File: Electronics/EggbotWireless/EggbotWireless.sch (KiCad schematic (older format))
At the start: 47 parts, among them J1 BATT, J2 Conn_01x04_Female, J3 USB_B_Micro, J4 AVR-ISP-6, Q1 FDD8447L, Q2 FDD8447L, U1 TPS62203DBV, U2 ATmega16A-AU, U3 DW01, U4 FS8205A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

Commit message: pcb prototype v0.1 (no steppers yet)
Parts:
- removed Q2: FDD8447L, Package_TO_SOT_SMD:TO-252-2, symbol Device:Q_NMOS_GDS
- added A1, A2: Pololu_Breakout_A4988, Module:Pololu_Breakout-16_15.2x20.3mm, symbol Driver_Motor:Pololu_Breakout_A4988
- added C14, C15: 100nf, Capacitor_SMD:C_0805_2012Metric_Pad1.15x1.40mm_HandSolder, symbol EggbotWireless-rescue:C-Device-Catfi-rescue
- added J5: Conn_01x03_Female, Connector_PinSocket_2.54mm:PinSocket_1x03_P2.54mm_Vertical, symbol Connector:Conn_01x03_Female
- added M1, M2: Stepper_Motor_bipolar, Connector_PinSocket_2.54mm:PinSocket_1x04_P2.54mm_Horizontal, symbol Motor:Stepper_Motor_bipolar
- added R17, R18: 10K, Resistor_SMD:R_0805_2012Metric_Pad1.15x1.40mm_HandSolder, symbol EggbotWireless-rescue:R-Device-Catfi-rescue
- U5: value INTERFACE-CP2102-GMR(QFN28) -> CP2102-GMR
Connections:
- net labels added: SCL, SDA
- wire segments 160 -> 165
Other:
- moved on the sheet: C7, C8, J2, J3, R6, R7, U5, U6

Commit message: change stepper driver to drv8825
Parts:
- removed A1, A2: Pololu_Breakout_A4988, Module:Pololu_Breakout-16_15.2x20.3mm, symbol Driver_Motor:Pololu_Breakout_A4988
- added A1, A2: Pololu_Breakout_DRV8825, Module:Pololu_Breakout-16_15.2x20.3mm, symbol Driver_Motor:Pololu_Breakout_DRV8825
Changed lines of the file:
@@
-	1    0    0    -1
-$EndComp
-$Comp
-L Driver_Motor:Pololu_Breakout_A4988 A1
-U 1 1 5CE85B52
-P 5100 3550
-F 0 "A1" H 5150 4431 50  0000 C CNN
-F 1 "Pololu_Breakout_A4988" H 5150 4340 50  0000 C CNN
-F 2 "Module:Pololu_Breakout-16_15.2x20.3mm" H 5375 2800 50  0001 L CNN
-F 3 "https://www.pololu.com/product/2980/pictures" H 5200 3250 50  0001 C CNN
-	1    5100 3550
 	1    0    0    -1
 $EndComp
@@
 	1    3600 2800
 	-1   0    0    1
-$EndComp
-$Comp
-L Driver_Motor:Pololu_Breakout_A4988 A2
-U 1 1 5CE843A9
-P 5150 5500
-F 0 "A2" H 5200 6381 50  0000 C CNN
-F 1 "Pololu_Breakout_A4988" H 5200 6290 50  0000 C CNN
-F 2 "Module:Pololu_Breakout-16_15.2x20.3mm" H 5425 4750 50  0001 L CNN
-F 3 "https://www.pololu.com/product/2980/pictures" H 5250 5200 50  0001 C CNN
-	1    5150 5500
-	1    0    0    -1
 $EndComp
 $Comp
@@
 Wire Wire Line
 	9100 5150 9100 5250
+$Comp
+L Driver_Motor:Pololu_Breakout_DRV8825 A1
+U 1 1 5CE88FAE
+P 5050 4150
+F 0 "A1" H 5050 4931 50  0000 C CNN
+F 1 "Pololu_Breakout_DRV8825" H 5050 4840 50  0000 C CNN
+F 2 "Module:Pololu_Breakout-16_15.2x20.3mm" H 5250 3350 50  0001 L CNN
+F 3 "https://www.pololu.com/product/2982" H 5150 3850 50  0001 C CNN
+	1    5050 4150
+	1    0    0    -1
+$EndComp
+$Comp
+L Driver_Motor:Pololu_Breakout_DRV8825 A2
+U 1 1 5CE8A6D5
+P 5050 5850
+F 0 "A2" H 5050 6631 50  0000 C CNN
+F 1 "Pololu_Breakout_DRV8825" H 5050 6540 50  0000 C CNN
+F 2 "Module:Pololu_Breakout-16_15.2x20.3mm" H 5250 5050 50  0001 L CNN
+F 3 "https://www.pololu.com/product/2982" H 5150 5550 50  0001 C CNN
+	1    5050 5850
+	1    0    0    -1
+$EndComp
 $EndSCHEMATC

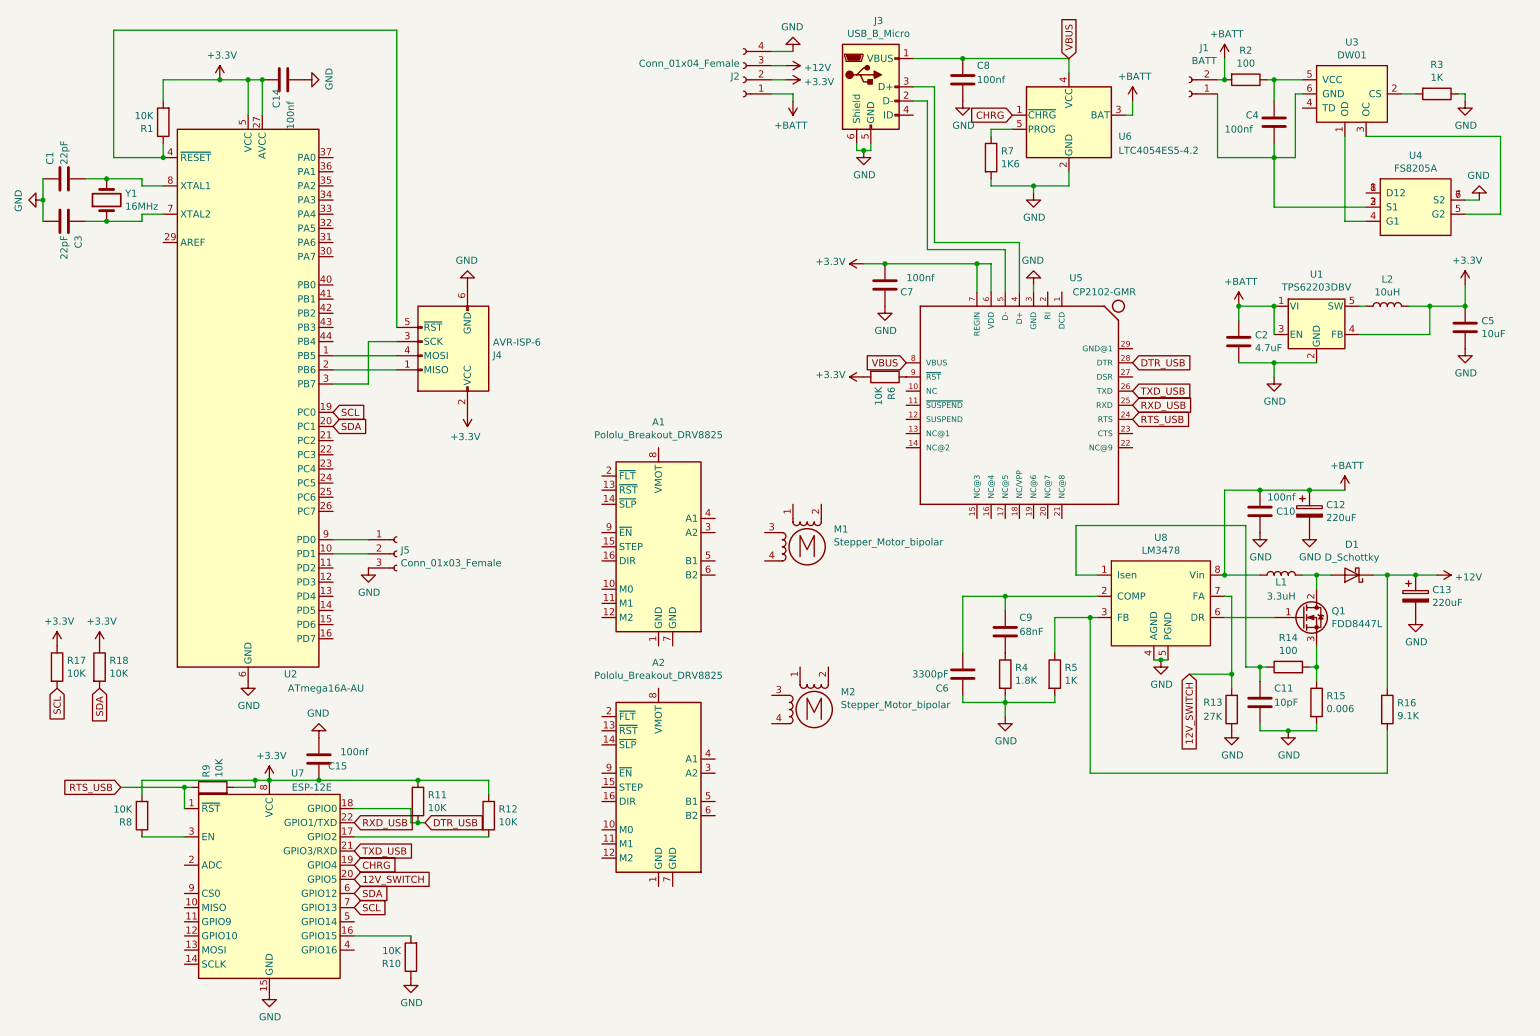
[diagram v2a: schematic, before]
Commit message: add steppers to the board
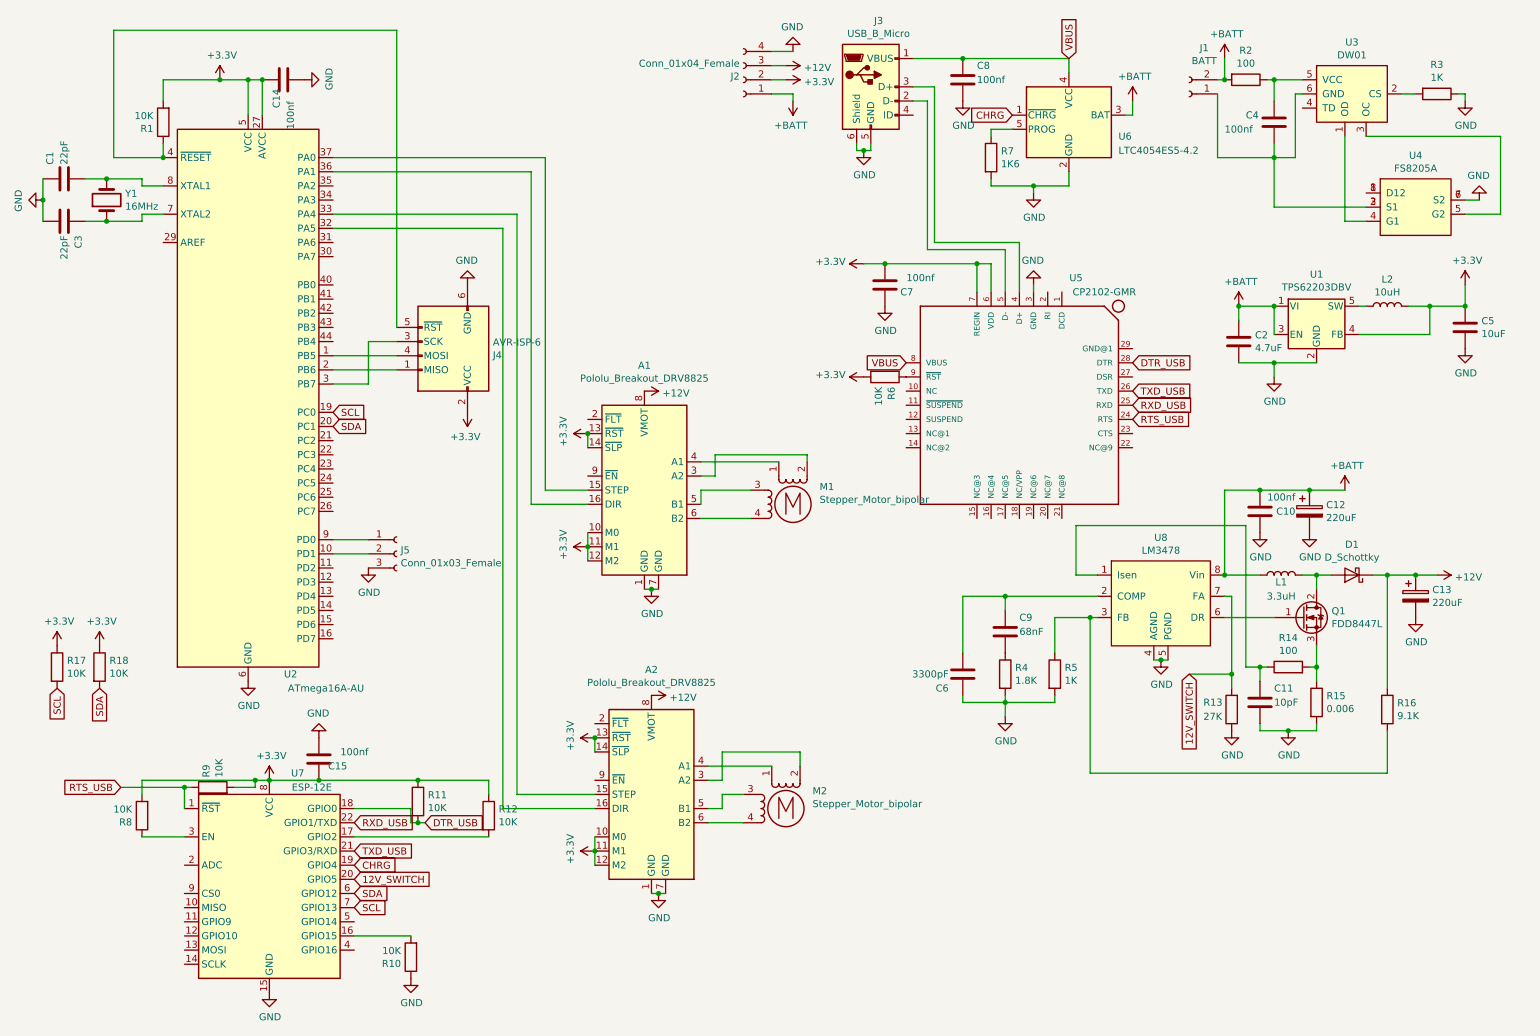
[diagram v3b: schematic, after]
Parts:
- M1, M2: footprint Connector_PinSocket_2.54mm:PinSocket_1x04_P2.54mm_Horizontal -> Connector_PinSocket_2.54mm:PinSocket_1x04_P2.54mm_Vertical
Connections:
- net +12V: now also A1.8 (VMOT), A2.8 (VMOT)
- net +3V3: now also A1.10 (M0), A1.11 (M1), A1.12 (M2), A1.13 (~RST), A1.14 (~SLP), A2.10 (M0), A2.11 (M1), A2.12 (M2), A2.13 (~RST), A2.14 (~SLP)
- net GND: now also A1.1 (GND), A1.7 (GND), A2.1 (GND), A2.7 (GND)
- net at A1.15 (STEP): now also U2.37 (PA0)
- net at A1.16 (DIR): now also U2.36 (PA1)
- net at A1.3 (A2): now also M1.2 (-)
- net at A1.4 (A1): now also M1.1
- net at A1.5 (B1): now also M1.3
- net at A1.6 (B2): now also M1.4
- net at A2.15 (STEP): now also U2.33 (PA4)
- net at A2.16 (DIR): now also U2.32 (PA5)
- net at A2.3 (A2): now also M2.2 (-)
- net at A2.4 (A1): now also M2.1
- net at A2.5 (B1): now also M2.3
- net at A2.6 (B2): now also M2.4
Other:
- moved on the sheet: A1, A2, M1, M2
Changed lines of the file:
@@
 L Motor:Stepper_Motor_bipolar M1
 U 1 1 5CF4B0D1
-P 6100 4250
-F 0 "M1" H 6288 4374 50  0000 L CNN
-F 1 "Stepper_Motor_bipolar" H 6288 4283 50  0000 L CNN
-F 2 "Connector_PinSocket_2.54mm:PinSocket_1x04_P2.54mm_Horizontal" H 6110 4240 50  0001 C CNN
-F 3 "http://www.infineon.com/dgdl/Application-Note-TLE8110EE_driving_UniPolarStepperMotor_V1.1.pdf?fileId=db3a30431be39b97011be5d0aa0a00b0" H 6110 4240 50  0001 C CNN
-	1    6100 4250
+P 6000 3950
+F 0 "M1" H 6188 4074 50  0000 L CNN
+F 1 "Stepper_Motor_bipolar" H 6188 3983 50  0000 L CNN
+F 2 "Connector_PinSocket_2.54mm:PinSocket_1x04_P2.54mm_Vertical" H 6010 3940 50  0001 C CNN
+F 3 "http://www.infineon.com/dgdl/Application-Note-TLE8110EE_driving_UniPolarStepperMotor_V1.1.pdf?fileId=db3a30431be39b97011be5d0aa0a00b0" H 6010 3940 50  0001 C CNN
+	1    6000 3950
 	1    0    0    -1
 $EndComp
@@
 L Motor:Stepper_Motor_bipolar M2
 U 1 1 5CF4C34B
-P 6150 5400
-F 0 "M2" H 6338 5524 50  0000 L CNN
-F 1 "Stepper_Motor_bipolar" H 6338 5433 50  0000 L CNN
-F 2 "Connector_PinSocket_2.54mm:PinSocket_1x04_P2.54mm_Horizontal" H 6160 5390 50  0001 C CNN
-F 3 "http://www.infineon.com/dgdl/Application-Note-TLE8110EE_driving_UniPolarStepperMotor_V1.1.pdf?fileId=db3a30431be39b97011be5d0aa0a00b0" H 6160 5390 50  0001 C CNN
-	1    6150 5400
+P 5950 6100
+F 0 "M2" H 6138 6224 50  0000 L CNN
+F 1 "Stepper_Motor_bipolar" H 6138 6133 50  0000 L CNN
+F 2 "Connector_PinSocket_2.54mm:PinSocket_1x04_P2.54mm_Vertical" H 5960 6090 50  0001 C CNN
+F 3 "http://www.infineon.com/dgdl/Application-Note-TLE8110EE_driving_UniPolarStepperMotor_V1.1.pdf?fileId=db3a30431be39b97011be5d0aa0a00b0" H 5960 6090 50  0001 C CNN
+	1    5950 6100
 	1    0    0    -1
 $EndComp
@@
 L Driver_Motor:Pololu_Breakout_DRV8825 A1
 U 1 1 5CE88FAE
-P 5050 4150
-F 0 "A1" H 5050 4931 50  0000 C CNN
-F 1 "Pololu_Breakout_DRV8825" H 5050 4840 50  0000 C CNN
-F 2 "Module:Pololu_Breakout-16_15.2x20.3mm" H 5250 3350 50  0001 L CNN
-F 3 "https://www.pololu.com/product/2982" H 5150 3850 50  0001 C CNN
-	1    5050 4150
+P 4950 3750
+F 0 "A1" H 4950 4531 50  0000 C CNN
+F 1 "Pololu_Breakout_DRV8825" H 4950 4440 50  0000 C CNN
+F 2 "Module:Pololu_Breakout-16_15.2x20.3mm" H 5150 2950 50  0001 L CNN
+F 3 "https://www.pololu.com/product/2982" H 5050 3450 50  0001 C CNN
+	1    4950 3750
 	1    0    0    -1
 $EndComp
@@
 L Driver_Motor:Pololu_Breakout_DRV8825 A2
 U 1 1 5CE8A6D5
-P 5050 5850
-F 0 "A2" H 5050 6631 50  0000 C CNN
-F 1 "Pololu_Breakout_DRV8825" H 5050 6540 50  0000 C CNN
-F 2 "Module:Pololu_Breakout-16_15.2x20.3mm" H 5250 5050 50  0001 L CNN
-F 3 "https://www.pololu.com/product/2982" H 5150 5550 50  0001 C CNN
-	1    5050 5850
-	1    0    0    -1
-$EndComp
+P 5000 5900
+F 0 "A2" H 5000 6681 50  0000 C CNN
+F 1 "Pololu_Breakout_DRV8825" H 5000 6590 50  0000 C CNN
+F 2 "Module:Pololu_Breakout-16_15.2x20.3mm" H 5200 5100 50  0001 L CNN
+F 3 "https://www.pololu.com/product/2982" H 5100 5600 50  0001 C CNN
+	1    5000 5900
+	1    0    0    -1
+$EndComp
+Wire Wire Line
+	5350 3650 5900 3650
+Wire Wire Line
+	6100 3650 6100 3600
+Wire Wire Line
+	6100 3600 5450 3600
+Wire Wire Line
+	5450 3600 5450 3750
+Wire Wire Line
+	5450 3750 5350 3750
+Wire Wire Line
+	5700 3850 5350 3850
+Wire Wire Line
+	5350 3850 5350 3950
+Wire Wire Line
+	5700 4050 5350 4050
+Wire Wire Line
+	5850 5800 5400 5800
+Wire Wire Line
+	6050 5800 6050 5700
+Wire Wire Line
+	6050 5700 5500 5700
+Wire Wire Line
+	5500 5700 5500 5900
+Wire Wire Line
+	5500 5900 5400 5900
+Wire Wire Line
+	5650 6000 5500 6000
+Wire Wire Line
+	5500 6000 5500 6100
+Wire Wire Line
+	5500 6100 5400 6100
+Wire Wire Line
+	5650 6200 5400 6200
+$Comp
+L power:+12V #PWR?
+U 1 1 5CF0714E
+P 5000 5300
+F 0 "#PWR?" H 5000 5150 50  0001 C CNN
+F 1 "+12V" V 5015 5428 50  0000 L CNN
+F 2 "" H 5000 5300 50  0001 C CNN
+F 3 "" H 5000 5300 50  0001 C CNN
+	1    5000 5300
+	0    1    1    0
+$EndComp
+$Comp
+L power:+12V #PWR?
+U 1 1 5CF093C7
+P 4950 3150
+F 0 "#PWR?" H 4950 3000 50  0001 C CNN
+F 1 "+12V" V 4965 3278 50  0000 L CNN
+F 2 "" H 4950 3150 50  0001 C CNN
+F 3 "" H 4950 3150 50  0001 C CNN
+	1    4950 3150
+	0    1    1    0
+$EndComp
+$Comp
+L EggbotWireless-rescue:GND-power-Catfi-rescue #PWR?
+U 1 1 5CF0A85A
+P 5050 6700
+F 0 "#PWR?" H 5050 6450 50  0001 C CNN
+F 1 "GND" H 5055 6527 50  0000 C CNN
+F 2 "" H 5050 6700 50  0001 C CNN
+F 3 "" H 5050 6700 50  0001 C CNN
+	1    5050 6700
+	1    0    0    -1
+$EndComp
+Wire Wire Line
+	5100 6700 5050 6700
+Wire Wire Line
+	5000 6700 5050 6700
+Connection ~ 5050 6700
+$Comp
+L EggbotWireless-rescue:GND-power-Catfi-rescue #PWR?
+U 1 1 5CF20CA3
+P 5000 4550
+F 0 "#PWR?" H 5000 4300 50  0001 C CNN
+F 1 "GND" H 5005 4377 50  0000 C CNN
+F 2 "" H 5000 4550 50  0001 C CNN
+F 3 "" H 5000 4550 50  0001 C CNN
+	1    5000 4550
+	1    0    0    -1
+$EndComp
+Wire Wire Line
+	5050 4550 5000 4550
+Wire Wire Line
+	4950 4550 5000 4550
+Connection ~ 5000 4550
+Wire Wire Line
+	4600 6300 4600 6400
+Connection ~ 4600 6400
+Wire Wire Line
+	4600 6400 4600 6500
+Wire Wire Line
+	4550 4350 4550 4250
+Wire Wire Line
+	4550 4150 4550 4250
+Connection ~ 4550 4250
+$Comp
+L power:+3.3V #PWR?
+U 1 1 5CF86B51
+P 4600 6400
+F 0 "#PWR?" H 4600 6250 50  0001 C CNN
+F 1 "+3.3V" H 4615 6573 50  0000 C CNN
+F 2 "" H 4600 6400 50  0001 C CNN
+F 3 "" H 4600 6400 50  0001 C CNN
+	1    4600 6400
+	0    -1   -1   0
+$EndComp
+$Comp
+L power:+3.3V #PWR?
+U 1 1 5CF8577A
+P 4550 4250
+F 0 "#PWR?" H 4550 4100 50  0001 C CNN
+F 1 "+3.3V" H 4565 4423 50  0000 C CNN
+F 2 "" H 4550 4250 50  0001 C CNN
+F 3 "" H 4550 4250 50  0001 C CNN
+	1    4550 4250
+	0    -1   -1   0
+$EndComp
+$Comp
+L power:+3.3V #PWR?
+U 1 1 5CF94114
+P 4600 5600
+F 0 "#PWR?" H 4600 5450 50  0001 C CNN
+F 1 "+3.3V" H 4615 5773 50  0000 C CNN
+F 2 "" H 4600 5600 50  0001 C CNN
+F 3 "" H 4600 5600 50  0001 C CNN
+	1    4600 5600
+	0    -1   -1   0
+$EndComp
+Wire Wire Line
+	4600 5600 4600 5700
+Connection ~ 4600 5600
+$Comp
+L power:+3.3V #PWR?
+U 1 1 5CFA006C
+P 4550 3450
+F 0 "#PWR?" H 4550 3300 50  0001 C CNN
+F 1 "+3.3V" H 4565 3623 50  0000 C CNN
+F 2 "" H 4550 3450 50  0001 C CNN
+F 3 "" H 4550 3450 50  0001 C CNN
+	1    4550 3450
+	0    -1   -1   0
+$EndComp
+Wire Wire Line
+	4550 3450 4550 3550
+Connection ~ 4550 3450
+Wire Wire Line
+	4550 3850 4250 3850
+Wire Wire Line
+	4250 3850 4250 1500
+Wire Wire Line
+	4250 1500 2750 1500
+Wire Wire Line
+	4550 3950 4150 3950
+Wire Wire Line
+	4150 3950 4150 1600
+Wire Wire Line
+	4150 1600 2750 1600
+Wire Wire Line
+	4600 6000 4050 6000
+Wire Wire Line
+	4050 6000 4050 1900
+Wire Wire Line
+	4050 1900 2750 1900
+Wire Wire Line
+	4600 6100 3950 6100
+Wire Wire Line
+	3950 6100 3950 2000
+Wire Wire Line
+	3950 2000 2750 2000
 $EndSCHEMATC

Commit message: add branding
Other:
- moved on the sheet: A2, M2
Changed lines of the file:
@@
 L Motor:Stepper_Motor_bipolar M2
 U 1 1 5CF4C34B
-P 5950 6100
-F 0 "M2" H 6138 6224 50  0000 L CNN
-F 1 "Stepper_Motor_bipolar" H 6138 6133 50  0000 L CNN
-F 2 "Connector_PinSocket_2.54mm:PinSocket_1x04_P2.54mm_Vertical" H 5960 6090 50  0001 C CNN
-F 3 "http://www.infineon.com/dgdl/Application-Note-TLE8110EE_driving_UniPolarStepperMotor_V1.1.pdf?fileId=db3a30431be39b97011be5d0aa0a00b0" H 5960 6090 50  0001 C CNN
-	1    5950 6100
+P 5950 5800
+F 0 "M2" H 6138 5924 50  0000 L CNN
+F 1 "Stepper_Motor_bipolar" H 6138 5833 50  0000 L CNN
+F 2 "Connector_PinSocket_2.54mm:PinSocket_1x04_P2.54mm_Vertical" H 5960 5790 50  0001 C CNN
+F 3 "http://www.infineon.com/dgdl/Application-Note-TLE8110EE_driving_UniPolarStepperMotor_V1.1.pdf?fileId=db3a30431be39b97011be5d0aa0a00b0" H 5960 5790 50  0001 C CNN
+	1    5950 5800
 	1    0    0    -1
 $EndComp
@@
 L Driver_Motor:Pololu_Breakout_DRV8825 A2
 U 1 1 5CE8A6D5
-P 5000 5900
-F 0 "A2" H 5000 6681 50  0000 C CNN
-F 1 "Pololu_Breakout_DRV8825" H 5000 6590 50  0000 C CNN
-F 2 "Module:Pololu_Breakout-16_15.2x20.3mm" H 5200 5100 50  0001 L CNN
-F 3 "https://www.pololu.com/product/2982" H 5100 5600 50  0001 C CNN
-	1    5000 5900
+P 5000 5600
+F 0 "A2" H 5000 6381 50  0000 C CNN
+F 1 "Pololu_Breakout_DRV8825" H 5000 6290 50  0000 C CNN
+F 2 "Module:Pololu_Breakout-16_15.2x20.3mm" H 5200 4800 50  0001 L CNN
+F 3 "https://www.pololu.com/product/2982" H 5100 5300 50  0001 C CNN
+	1    5000 5600
 	1    0    0    -1
 $EndComp
@@
 	5700 4050 5350 4050
 Wire Wire Line
-	5850 5800 5400 5800
-Wire Wire Line
-	6050 5800 6050 5700
-Wire Wire Line
-	6050 5700 5500 5700
-Wire Wire Line
-	5500 5700 5500 5900
-Wire Wire Line
-	5500 5900 5400 5900
-Wire Wire Line
-	5650 6000 5500 6000
-Wire Wire Line
-	5500 6000 5500 6100
-Wire Wire Line
-	5500 6100 5400 6100
-Wire Wire Line
-	5650 6200 5400 6200
+	5850 5500 5400 5500
+Wire Wire Line
+	6050 5500 6050 5400
+Wire Wire Line
+	6050 5400 5500 5400
+Wire Wire Line
+	5500 5400 5500 5600
+Wire Wire Line
+	5500 5600 5400 5600
+Wire Wire Line
+	5650 5700 5500 5700
+Wire Wire Line
+	5500 5700 5500 5800
+Wire Wire Line
+	5500 5800 5400 5800
+Wire Wire Line
+	5650 5900 5400 5900
 $Comp
 L power:+12V #PWR?
 U 1 1 5CF0714E
-P 5000 5300
-F 0 "#PWR?" H 5000 5150 50  0001 C CNN
-F 1 "+12V" V 5015 5428 50  0000 L CNN
-F 2 "" H 5000 5300 50  0001 C CNN
-F 3 "" H 5000 5300 50  0001 C CNN
-	1    5000 5300
+P 5000 5000
+F 0 "#PWR?" H 5000 4850 50  0001 C CNN
+F 1 "+12V" V 5015 5128 50  0000 L CNN
+F 2 "" H 5000 5000 50  0001 C CNN
+F 3 "" H 5000 5000 50  0001 C CNN
+	1    5000 5000
 	0    1    1    0
 $EndComp
@@
 L EggbotWireless-rescue:GND-power-Catfi-rescue #PWR?
 U 1 1 5CF0A85A
-P 5050 6700
-F 0 "#PWR?" H 5050 6450 50  0001 C CNN
-F 1 "GND" H 5055 6527 50  0000 C CNN
-F 2 "" H 5050 6700 50  0001 C CNN
-F 3 "" H 5050 6700 50  0001 C CNN
-	1    5050 6700
-	1    0    0    -1
-$EndComp
-Wire Wire Line
-	5100 6700 5050 6700
-Wire Wire Line
-	5000 6700 5050 6700
-Connection ~ 5050 6700
+P 5050 6400
+F 0 "#PWR?" H 5050 6150 50  0001 C CNN
+F 1 "GND" H 5055 6227 50  0000 C CNN
+F 2 "" H 5050 6400 50  0001 C CNN
+F 3 "" H 5050 6400 50  0001 C CNN
+	1    5050 6400
+	1    0    0    -1
+$EndComp
+Wire Wire Line
+	5100 6400 5050 6400
+Wire Wire Line
+	5000 6400 5050 6400
+Connection ~ 5050 6400
 $Comp
 L EggbotWireless-rescue:GND-power-Catfi-rescue #PWR?
@@
 Connection ~ 5000 4550
 Wire Wire Line
-	4600 6300 4600 6400
-Connection ~ 4600 6400
-Wire Wire Line
-	4600 6400 4600 6500
+	4600 6000 4600 6100
+Connection ~ 4600 6100
+Wire Wire Line
+	4600 6100 4600 6200
 Wire Wire Line
 	4550 4350 4550 4250
@@
 L power:+3.3V #PWR?
 U 1 1 5CF86B51
-P 4600 6400
-F 0 "#PWR?" H 4600 6250 50  0001 C CNN
-F 1 "+3.3V" H 4615 6573 50  0000 C CNN
-F 2 "" H 4600 6400 50  0001 C CNN
-F 3 "" H 4600 6400 50  0001 C CNN
-	1    4600 6400
+P 4600 6100
+F 0 "#PWR?" H 4600 5950 50  0001 C CNN
+F 1 "+3.3V" H 4615 6273 50  0000 C CNN
+F 2 "" H 4600 6100 50  0001 C CNN
+F 3 "" H 4600 6100 50  0001 C CNN
+	1    4600 6100
 	0    -1   -1   0
 $EndComp
@@
 L power:+3.3V #PWR?
 U 1 1 5CF94114
-P 4600 5600
-F 0 "#PWR?" H 4600 5450 50  0001 C CNN
-F 1 "+3.3V" H 4615 5773 50  0000 C CNN
-F 2 "" H 4600 5600 50  0001 C CNN
-F 3 "" H 4600 5600 50  0001 C CNN
-	1    4600 5600
-	0    -1   -1   0
-$EndComp
-Wire Wire Line
-	4600 5600 4600 5700
-Connection ~ 4600 5600
+P 4600 5300
+F 0 "#PWR?" H 4600 5150 50  0001 C CNN
+F 1 "+3.3V" H 4615 5473 50  0000 C CNN
+F 2 "" H 4600 5300 50  0001 C CNN
+F 3 "" H 4600 5300 50  0001 C CNN
+	1    4600 5300
+	0    -1   -1   0
+$EndComp
+Wire Wire Line
+	4600 5300 4600 5400
+Connection ~ 4600 5300
 $Comp
 L power:+3.3V #PWR?
@@
 	4150 1600 2750 1600
 Wire Wire Line
-	4600 6000 4050 6000
-Wire Wire Line
-	4050 6000 4050 1900
+	4600 5700 4050 5700
 Wire Wire Line
 	4050 1900 2750 1900
 Wire Wire Line
-	4600 6100 3950 6100
-Wire Wire Line
-	3950 6100 3950 2000
+	4600 5800 3950 5800
 Wire Wire Line
 	3950 2000 2750 2000
+Wire Wire Line
+	4050 1900 4050 5700
+Wire Wire Line
+	3950 2000 3950 5800
 $EndSCHEMATC
